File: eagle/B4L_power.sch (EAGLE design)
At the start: 26 parts, among them IC1 LM2576HVT-12, Q1 STP40NF03L, U1 LM211P

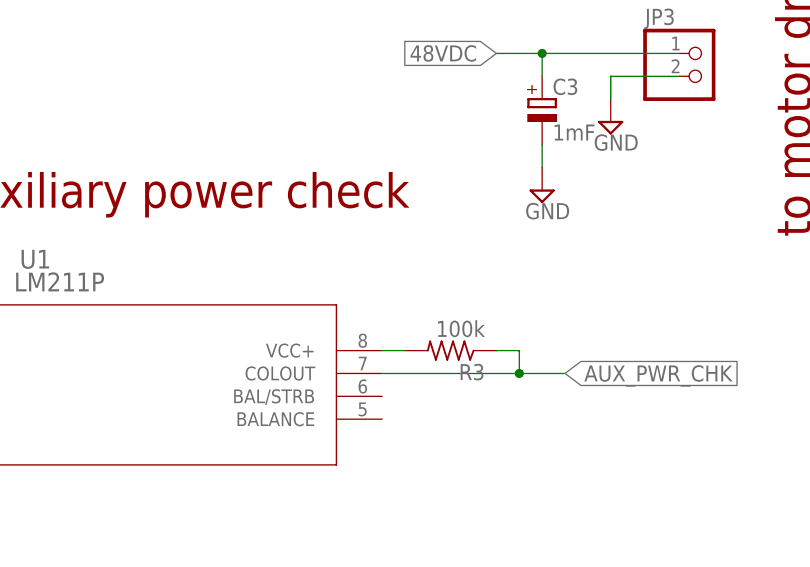
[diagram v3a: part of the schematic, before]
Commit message: Update PCB power for 48V supply
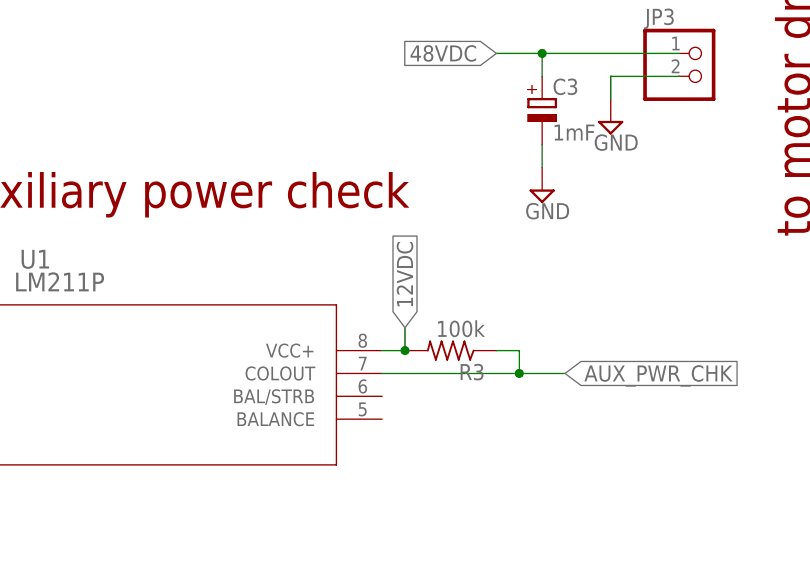
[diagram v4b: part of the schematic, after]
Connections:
- removed net N$4: R3.2, U1.VCC+
- net 12VDC: now also R3.2, U1.VCC+
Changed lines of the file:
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@@
 <label x="93.98" y="45.72" size="1.778" layer="95" rot="R90" xref="yes"/>
+</segment>
+<segment>
+<pinref part="U1" gate="A" pin="VCC+"/>
+<pinref part="R3" gate="G$1" pin="2"/>
+<wire x1="200.66" y1="60.96" x2="203.2" y2="60.96" width="0.1524" layer="91"/>
+<wire x1="203.2" y1="60.96" x2="203.2" y2="63.5" width="0.1524" layer="91"/>
+<junction x="203.2" y="60.96"/>
+<label x="203.2" y="63.5" size="1.778" layer="95" rot="R90" xref="yes"/>
 </segment>
 </net>
@@
 </segment>
 </net>
-<net name="N$4" class="0">
-<segment>
-<pinref part="U1" gate="A" pin="VCC+"/>
-<pinref part="R3" gate="G$1" pin="2"/>
-<wire x1="200.66" y1="60.96" x2="203.2" y2="60.96" width="0.1524" layer="91"/>
-</segment>
-</net>
